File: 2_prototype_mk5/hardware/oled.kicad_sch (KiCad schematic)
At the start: 1 part, among them J7 Conn_01x04_Pin

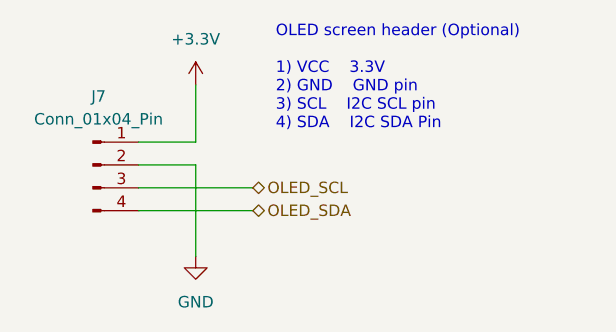
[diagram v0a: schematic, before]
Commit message: Major MKV redesign using embedded RP2350
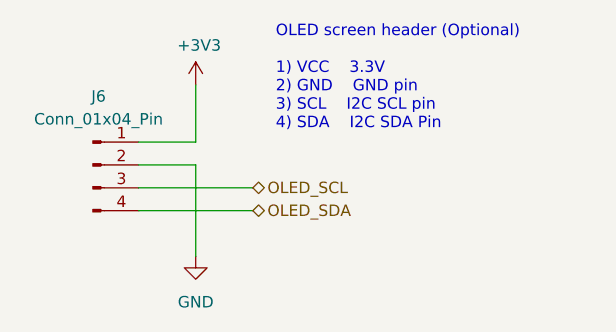
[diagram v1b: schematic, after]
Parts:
- renumbered J7 to J6
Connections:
- net +3.3V renamed +3V3
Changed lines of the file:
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@@
 		(dnp no)
 		(fields_autoplaced yes)
-		(property "Reference" "J7"
+		(property "Reference" "J6"
 			(at 128.905 86.36 0)
 			(show_name no)
@@
 			(project "HDD Synth Prototype MK5"
 				(path "/1a22431a-ba36-40a0-9a7e-c2a82ec69c53/4f2241a1-46db-49da-aeae-e06acaad5be6"
-					(reference "J7")
+					(reference "J6")
 					(unit 1)
 				)
@@
 		(dnp no)
 		(fields_autoplaced yes)
-		(property "Reference" "#PWR030"
+		(property "Reference" "#PWR048"
 			(at 139.7 110.49 0)
 			(hide yes)
@@
 			(project "HDD Synth Prototype MK5"
 				(path "/1a22431a-ba36-40a0-9a7e-c2a82ec69c53/4f2241a1-46db-49da-aeae-e06acaad5be6"
-					(reference "#PWR030")
+					(reference "#PWR048")
 					(unit 1)
 				)
@@
 	)
 	(symbol
-		(lib_id "power:+3.3V")
+		(lib_id "power:+3V3")
 		(at 139.7 85.09 0)
 		(unit 1)
@@
 		(in_pos_files yes)
 		(dnp no)
-		(fields_autoplaced yes)
-		(property "Reference" "#PWR025"
+		(property "Reference" "#PWR047"
 			(at 139.7 88.9 0)
 			(hide yes)
@@
 			)
 		)
-		(property "Value" "+3.3V"
-			(at 139.7 80.01 0)
+		(property "Value" "+3V3"
+			(at 140.081 80.6958 0)
 			(show_name no)
 			(do_not_autoplace no)
@@
 			)
 		)
-		(property "Description" "Power symbol creates a global label with name \"+3.3V\""
+		(property "Description" ""
 			(at 139.7 85.09 0)
-			(hide yes)
 			(show_name no)
 			(do_not_autoplace no)
@@
 			(project "HDD Synth Prototype MK5"
 				(path "/1a22431a-ba36-40a0-9a7e-c2a82ec69c53/4f2241a1-46db-49da-aeae-e06acaad5be6"
-					(reference "#PWR025")
+					(reference "#PWR047")
 					(unit 1)
 				)

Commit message: MKV: Add LCSC numbers and resolve DRC errors
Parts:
- J6: LCSC_Part_Number (none) -> C124378
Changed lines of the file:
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@@
+			)
+		)
+		(property "Availability" ""
+			(at 128.27 93.98 0)
+			(hide yes)
+			(show_name no)
+			(do_not_autoplace no)
+			(effects
+				(font
+					(size 1.27 1.27)
+				)
+			)
+		)
+		(property "Check_prices" ""
+			(at 128.27 93.98 0)
+			(hide yes)
+			(show_name no)
+			(do_not_autoplace no)
+			(effects
+				(font
+					(size 1.27 1.27)
+				)
+			)
+		)
+		(property "Comment" ""
+			(at 128.27 93.98 0)
+			(hide yes)
+			(show_name no)
+			(do_not_autoplace no)
+			(effects
+				(font
+					(size 1.27 1.27)
+				)
+			)
+		)
+		(property "EU_RoHS_Compliance" ""
+			(at 128.27 93.98 0)
+			(hide yes)
+			(show_name no)
+			(do_not_autoplace no)
+			(effects
+				(font
+					(size 1.27 1.27)
+				)
+			)
+		)
+		(property "MF" ""
+			(at 128.27 93.98 0)
+			(hide yes)
+			(show_name no)
+			(do_not_autoplace no)
+			(effects
+				(font
+					(size 1.27 1.27)
+				)
+			)
+		)
+		(property "MP" ""
+			(at 128.27 93.98 0)
+			(hide yes)
+			(show_name no)
+			(do_not_autoplace no)
+			(effects
+				(font
+					(size 1.27 1.27)
+				)
+			)
+		)
+		(property "PARTREV" ""
+			(at 128.27 93.98 0)
+			(hide yes)
+			(show_name no)
+			(do_not_autoplace no)
+			(effects
+				(font
+					(size 1.27 1.27)
+				)
+			)
+		)
+		(property "Package" ""
+			(at 128.27 93.98 0)
+			(hide yes)
+			(show_name no)
+			(do_not_autoplace no)
+			(effects
+				(font
+					(size 1.27 1.27)
+				)
+			)
+		)
+		(property "Price" ""
+			(at 128.27 93.98 0)
+			(hide yes)
+			(show_name no)
+			(do_not_autoplace no)
+			(effects
+				(font
+					(size 1.27 1.27)
+				)
+			)
+		)
+		(property "Purchase-URL" ""
+			(at 128.27 93.98 0)
+			(hide yes)
+			(show_name no)
+			(do_not_autoplace no)
+			(effects
+				(font
+					(size 1.27 1.27)
+				)
+			)
+		)
+		(property "STANDARD" ""
+			(at 128.27 93.98 0)
+			(hide yes)
+			(show_name no)
+			(do_not_autoplace no)
+			(effects
+				(font
+					(size 1.27 1.27)
+				)
+			)
+		)
+		(property "SnapEDA_Link" ""
+			(at 128.27 93.98 0)
+			(hide yes)
+			(show_name no)
+			(do_not_autoplace no)
+			(effects
+				(font
+					(size 1.27 1.27)
+				)
+			)
+		)
+		(property "LCSC_Part_Number" "C124378"
+			(at 128.27 93.98 0)
+			(hide yes)
+			(show_name no)
+			(do_not_autoplace no)
+			(effects
+				(font
+					(size 1.27 1.27)
+				)
 			)
 		)
